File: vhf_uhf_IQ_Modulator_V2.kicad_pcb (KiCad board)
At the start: 2 copper layers, 71 parts, among them J1 CONN_01X03, J2 TEST_1P, J3 Audio-Jack-3, J4 CONN_01X04, J5 SMA Edge FM, Q1 BC817-40, Q2 BC817-40, Q3 BC817-40, U1 TRF3701, U2 MMZ09332BT1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

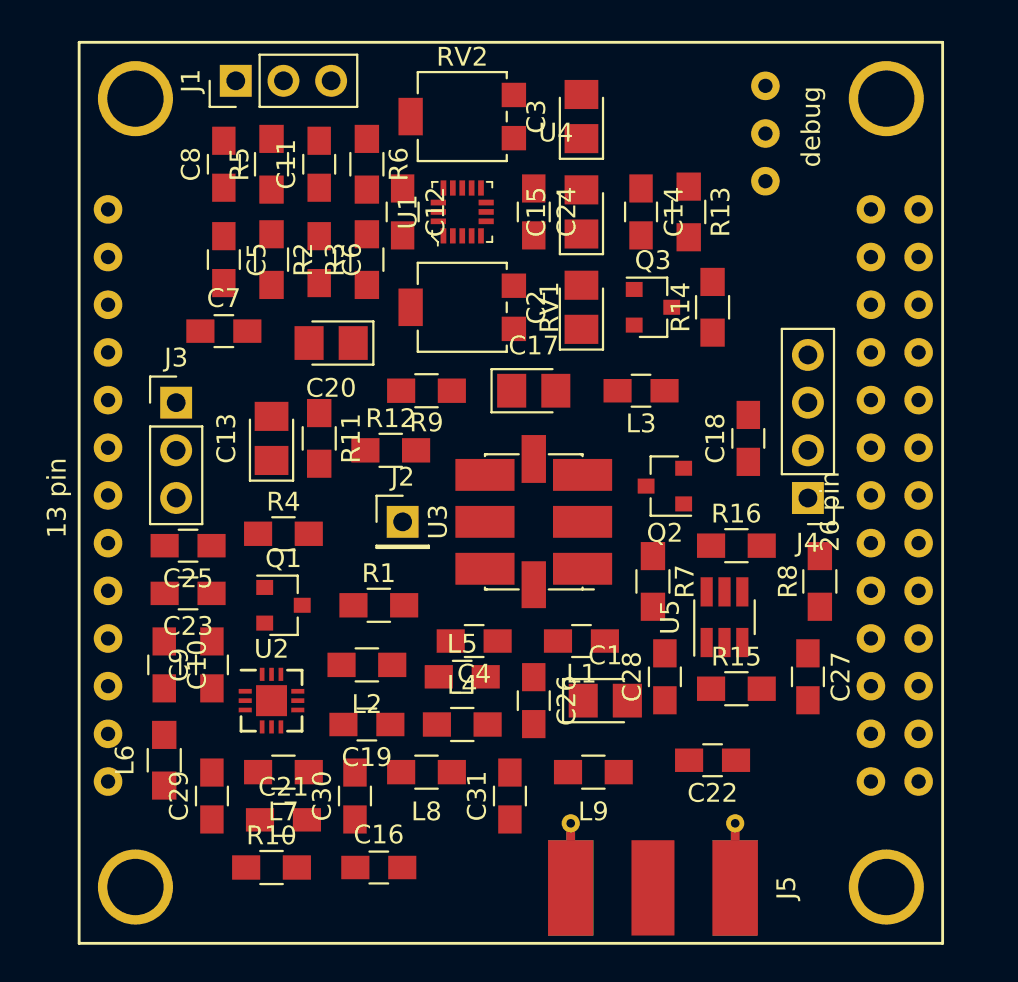
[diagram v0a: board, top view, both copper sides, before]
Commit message: Plasing labels
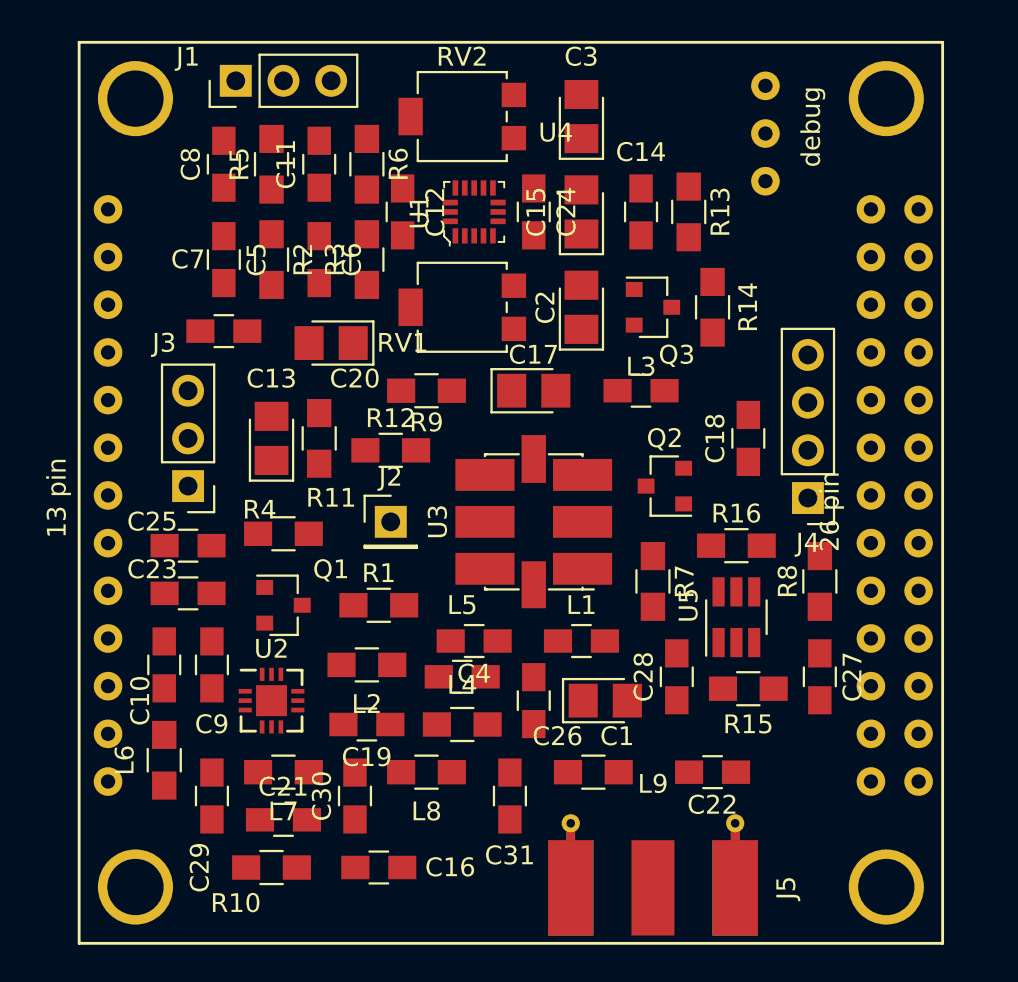
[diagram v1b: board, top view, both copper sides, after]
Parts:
- moved J3 4.49 mm to (154.3, 80.6), turned to 180 degrees
- moved C27 0.64 mm to (188.0, 90.8)
- moved J2 0.64 mm to (165.1, 82.5)
- moved R15 0.64 mm to (184.2, 91.4)
- moved C22 0.64 mm to (182.2, 95.9)
- moved C28 0.63 mm to (180.3, 90.8)
- moved U1 0.63 mm to (169.5, 66.0)
- moved U5 0.63 mm to (183.5, 87.6)
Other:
- net class +3V3 added: clearance 0.2, trace_width 0.3, via_dia 0.6, via_drill 0.4
- net class +5V added: clearance 0.2, trace_width 0.3, via_dia 0.6, via_drill 0.4

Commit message: Routing
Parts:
- moved L1 1.27 mm to (176.5, 88.9)
- moved C16 0.90 mm to (163.8, 101.6), turned to 180 degrees
- moved C21 0.64 mm to (159.4, 99.1)
- moved L2 0.64 mm to (163.8, 90.8)
- moved C4 0.63 mm to (168.9, 88.9)
- moved R1 0.63 mm to (163.8, 87.0)
- moved R10 0.63 mm to (158.8, 101.6)
- moved R7 0.63 mm to (179.1, 85.1)
- turned C7 to 180 degrees
- turned Q3 to 270 degrees
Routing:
- net GND: track 0.00 -> 184.4 mm, vias 0 -> 7
- net +5V: track 0.00 -> 116.1 mm, vias 0 -> 4
- net +3V3: track 0.00 -> 50.4 mm, vias 0 -> 3
- net Net-(C5-Pad1): track 0.00 -> 20.8 mm
- net Net-(C8-Pad1): track 0.00 -> 20.4 mm
- net Net-(C4-Pad2): track 0.00 -> 19.2 mm, vias 0 -> 3
- net Net-(C22-Pad2): track 0.00 -> 11.8 mm
- net Net-(C25-Pad2): track 0.00 -> 11.7 mm, vias 0 -> 1
- net Net-(C23-Pad1): track 0.00 -> 11.0 mm
- net Net-(R4-Pad1): track 0.00 -> 8.04 mm
- net Net-(Q2-Pad3): track 0.00 -> 7.49 mm
- net Net-(R11-Pad2): track 0.00 -> 7.46 mm
- net Net-(C7-Pad1): track 0.00 -> 7.39 mm
- net Net-(J5-Pad1): track 0.00 -> 6.92 mm
- net Net-(Q1-Pad3): track 0.00 -> 6.25 mm
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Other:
- net class +3V3: via_dia 0.6 -> 0.65; via_drill 0.4 -> 0.45
- net class +5V: via_dia 0.6 -> 0.65; via_drill 0.4 -> 0.45
- net class GND added: clearance 0.2, trace_width 0.3, via_dia 0.65, via_drill 0.45
- net class RF added: clearance 0.12, trace_width 0.36, via_dia 0.65, via_drill 0.45

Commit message: More rooting
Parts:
- moved C15 2.17 mm to (177.4, 65.8)
- moved C24 1.85 mm to (174.6, 65.8)
- moved C14 1.41 mm to (179.8, 65.8)
- moved R13 1.27 mm to (182.2, 66.0)
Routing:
- net GND: track 184.4 -> 225.9 mm, vias 7 -> 9
- net +3V3: track 50.4 -> 74.6 mm
- net SDA: track 0.00 -> 17.4 mm, vias 0 -> 2
- net Net-(C7-Pad1): track 7.39 -> 20.4 mm, vias 0 -> 2
- net +5V: track 116.1 -> 128.2 mm, vias 4 -> 6
- net Net-(R9-Pad1): track 0.00 -> 9.27 mm, vias 0 -> 2
- net Net-(Q2-Pad1): track 0.00 -> 9.04 mm, vias 0 -> 2
- net Net-(RV2-Pad2): track 0.00 -> 6.70 mm
- net Net-(Q3-Pad3): track 5.57 -> 7.01 mm, vias 0 -> 2
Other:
- net class +5V Small added: clearance 0.2, trace_width 0.25, via_dia 0.6, via_drill 0.4
- net class GND Small added: clearance 0.1, trace_width 0.3, via_dia 0.6, via_drill 0.4
- net class RF Small added: clearance 0.1, trace_width 0.305, via_dia 0.65, via_drill 0.45

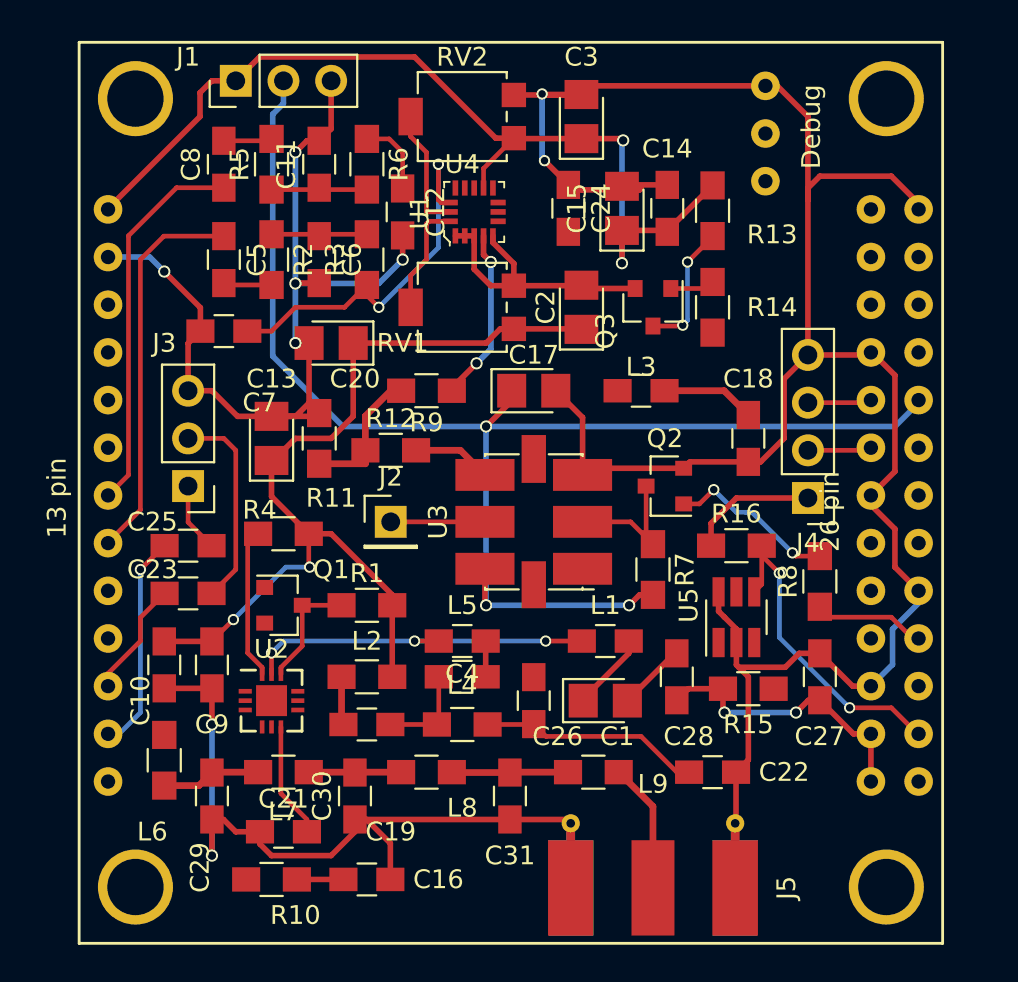
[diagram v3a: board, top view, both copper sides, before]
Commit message: 23 tracks left
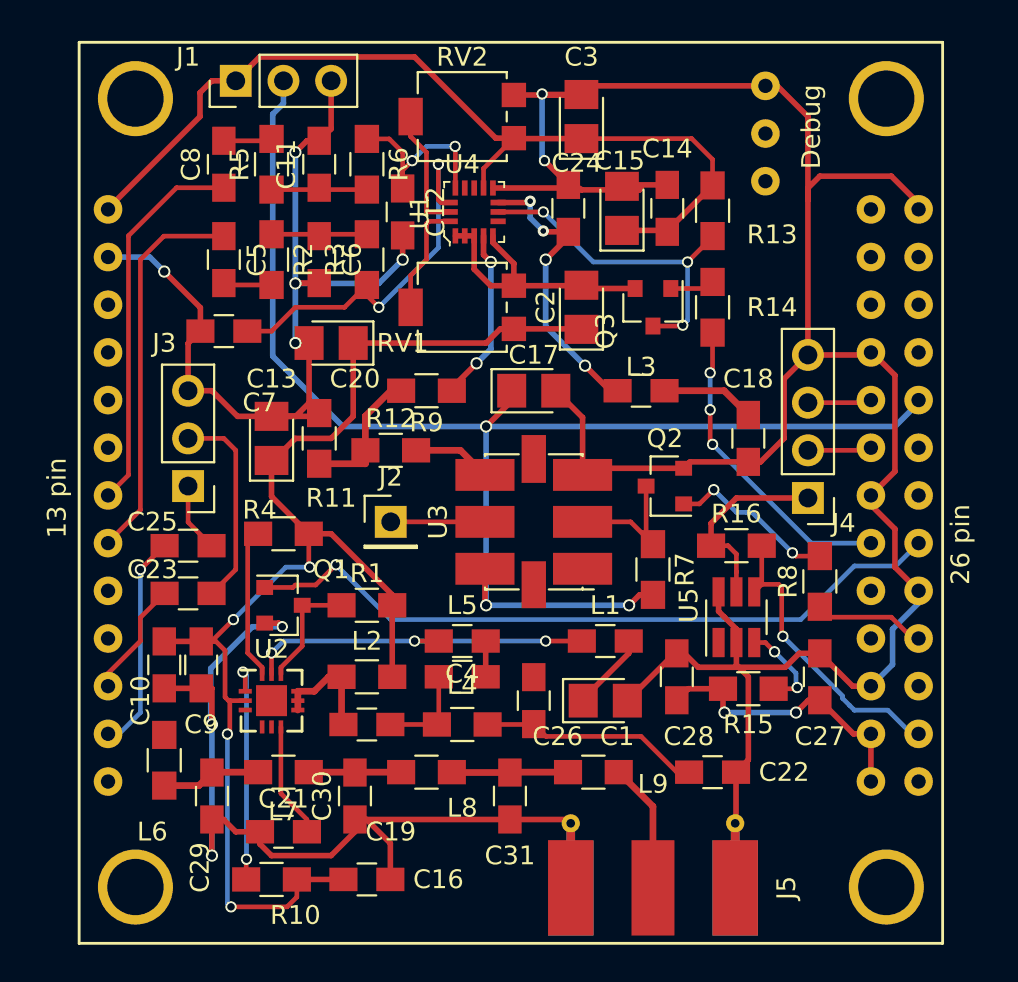
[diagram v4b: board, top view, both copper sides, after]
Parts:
- moved C9 0.57 mm to (155.0, 90.2)
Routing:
- net PA01: track 0.00 -> 38.2 mm, vias 0 -> 1
- net +5V: track 128.2 -> 150.9 mm
- net PA07: track 0.00 -> 16.7 mm, vias 0 -> 3
- net GND: track 225.9 -> 242.3 mm, vias 9 -> 10
- net Net-(C24-Pad2): track 0.00 -> 15.8 mm, vias 0 -> 4
- net Net-(R10-Pad1): track 0.00 -> 12.2 mm, vias 0 -> 2
- net Net-(Q3-Pad3): track 7.01 -> 18.2 mm, vias 2 -> 3
- net Net-(C12-Pad1): track 4.13 -> 10.6 mm, vias 0 -> 2
- net SLC: track 0.00 -> 4.97 mm, vias 0 -> 2
- net Net-(C19-Pad2): track 2.58 -> 6.23 mm
- net SDA: track 17.4 -> 16.4 mm, vias 2 -> 1
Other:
- net class +5V Small: clearance 0.2 -> 0.1
- net class RF Small: trace_width 0.305 -> 0.3; via_dia 0.65 -> 0.6; via_drill 0.45 -> 0.3

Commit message: 19 tracks left
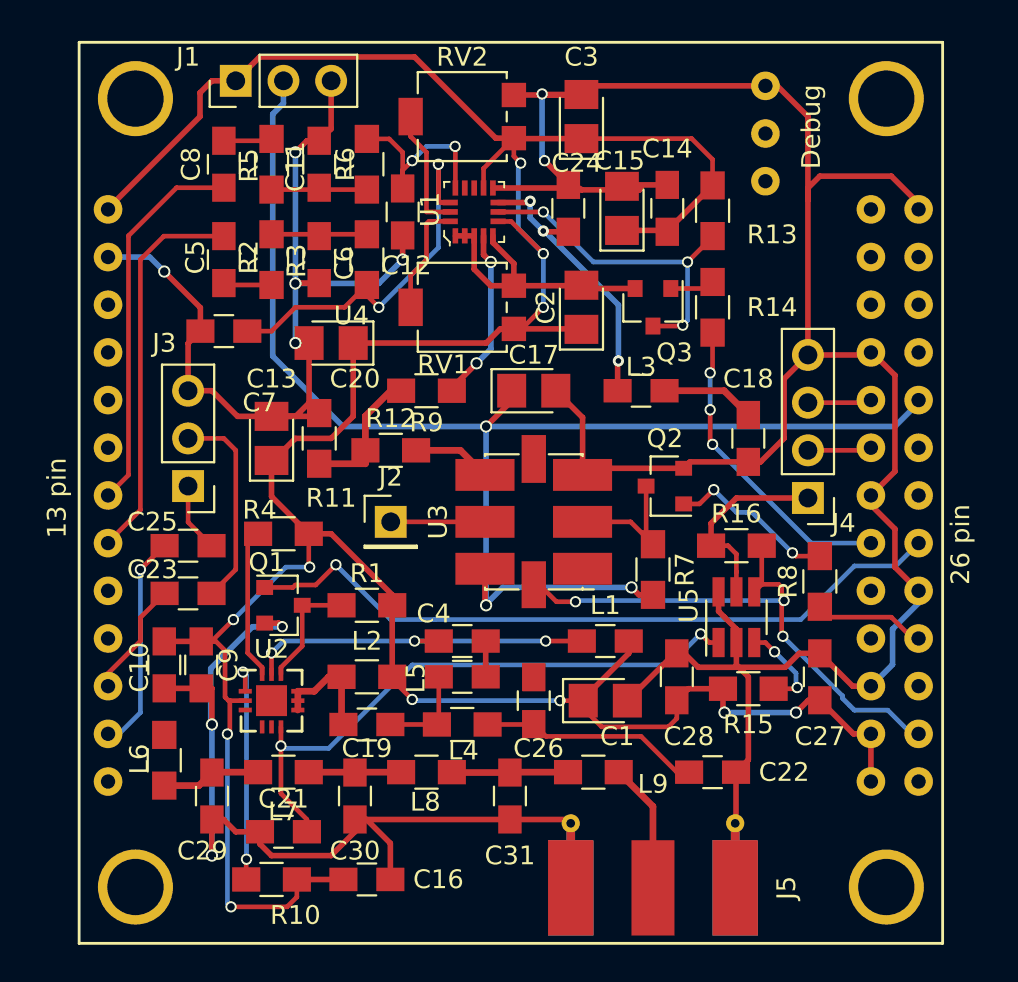
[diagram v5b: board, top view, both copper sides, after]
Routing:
- net +5V: track 150.9 -> 183.6 mm, vias 6 -> 11
- net PDet: track 6.16 -> 32.2 mm, vias 0 -> 2
- net SDA: track 16.4 -> 30.3 mm, vias 1 -> 3
- net Net-(C24-Pad2): track 15.8 -> 15.9 mm, vias 4 -> 3
